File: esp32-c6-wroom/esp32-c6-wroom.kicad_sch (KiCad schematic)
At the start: 1 part, among them U1 ESP32-C6-WROOM-1-N8

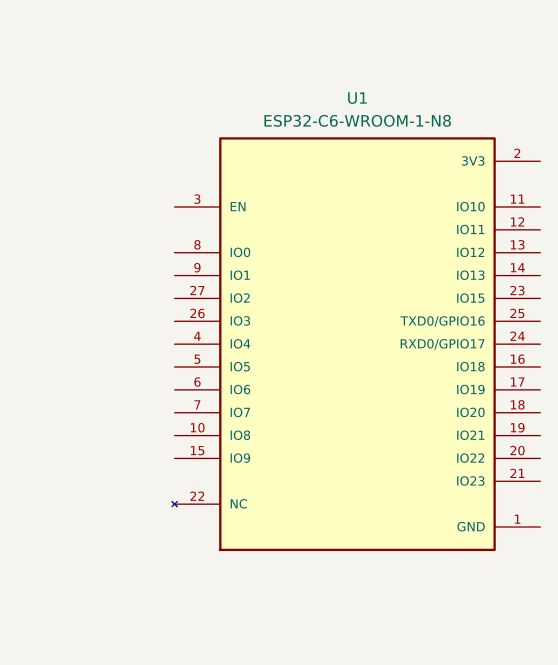
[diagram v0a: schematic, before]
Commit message: fix: use official espressif lib for esp32-c6 projects
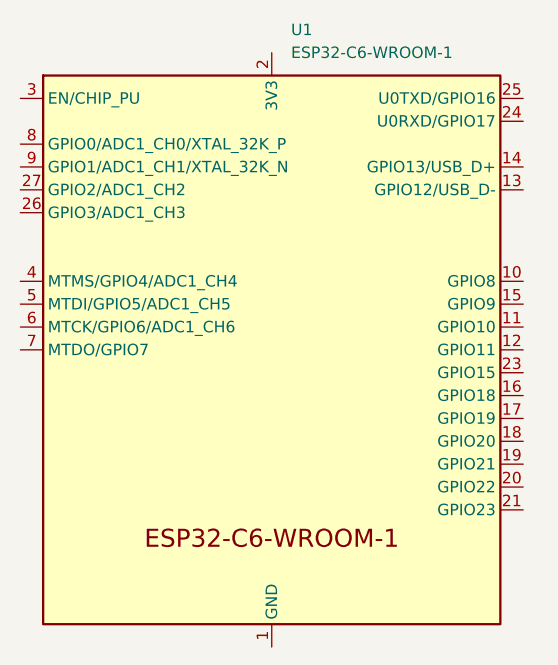
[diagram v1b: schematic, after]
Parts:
- removed U1: ESP32-C6-WROOM-1-N8, ESP32:XCVR_ESP32-C6-WROOM-1-N8, symbol ESP32:ESP32-C6-WROOM-1-N8
- added U1: ESP32-C6-WROOM-1, PCM_Espressif:ESP32-C6-WROOM-1, symbol PCM_Espressif:ESP32-C6-WROOM-1
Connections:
- new net: U1.1 (GND), U1.28 (GND), U1.29 (GND)
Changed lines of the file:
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@@
 	(paper "A4")
 	(symbol
-		(lib_id "ESP32:ESP32-C6-WROOM-1-N8")
-		(at 151.765 97.155 0)
+		(lib_id "PCM_Espressif:ESP32-C6-WROOM-1")
+		(at 142.24 97.79 0)
 		(unit 1)
 		(exclude_from_sim no)
@@
 		(fields_autoplaced yes)
 		(property "Reference" "U1"
-			(at 151.765 69.85 0)
+			(at 144.3833 62.23 0)
 			(effects
 				(font
 					(size 1.27 1.27)
 				)
+				(justify left)
 			)
 		)
-		(property "Value" "ESP32-C6-WROOM-1-N8"
-			(at 151.765 72.39 0)
+		(property "Value" "ESP32-C6-WROOM-1"
+			(at 144.3833 64.77 0)
 			(effects
 				(font
 					(size 1.27 1.27)
 				)
+				(justify left)
 			)
 		)
-		(property "Footprint" "ESP32:XCVR_ESP32-C6-WROOM-1-N8"
-			(at 151.765 97.155 0)
-			(effects
-				(font
-					(size 1.27 1.27)
-				)
-				(justify bottom)
-				(hide yes)
-			)
-		)
-		(property "Datasheet" ""
-			(at 151.765 97.155 0)
+		(property "Footprint" "PCM_Espressif:ESP32-C6-WROOM-1"
+			(at 142.24 142.875 0)
 			(effects
 				(font
@@
 			)
 		)
-		(property "Description" ""
-			(at 151.765 97.155 0)
+		(property "Datasheet" "https://www.espressif.com/sites/default/files/documentation/esp32-c6-wroom-1_wroom-1u_datasheet_en.pdf"
+			(at 142.24 146.05 0)
 			(effects
 				(font
@@
 			)
 		)
-		(property "MF" "Espressif Systems"
-			(at 151.765 97.155 0)
+		(property "Description" "ESP32-C6-WROOM-1/U is a module that supports 2.4 GHz Wi-Fi 6 (802.11 ax), Bluetooth® 5 (LE), Zigbee and Thread (802.15.4)"
+			(at 142.24 97.79 0)
 			(effects
 				(font
 					(size 1.27 1.27)
 				)
-				(justify bottom)
 				(hide yes)
 			)
 		)
-		(property "MAXIMUM_PACKAGE_HEIGHT" "3.25mm"
-			(at 151.765 97.155 0)
-			(effects
-				(font
-					(size 1.27 1.27)
-				)
-				(justify bottom)
-				(hide yes)
-			)
+		(pin "24"
 		)
-		(property "Package" "SMD-28 Espressif Systems"
-			(at 151.765 97.155 0)
-			(effects
-				(font
-					(size 1.27 1.27)
-				)
-				(justify bottom)
-				(hide yes)
-			)
+		(pin "26"
 		)
-		(property "Price" "None"
-			(at 151.765 97.155 0)
-			(effects
-				(font
-					(size 1.27 1.27)
-				)
-				(justify bottom)
-				(hide yes)
-			)
+		(pin "1"
 		)
-		(property "Check_prices" "https://www.snapeda.com/parts/ESP32-C6-WROOM-1-N8/Espressif+Systems/view-part/?ref=eda"
-			(at 151.765 97.155 0)
-			(effects
-				(font
-					(size 1.27 1.27)
-				)
-				(justify bottom)
-				(hide yes)
-			)
+		(pin "2"
 		)
-		(property "STANDARD" "Manufacturer Recommendations"
-			(at 151.765 97.155 0)
-			(effects
-				(font
-					(size 1.27 1.27)
-				)
-				(justify bottom)
-				(hide yes)
-			)
+		(pin "9"
 		)
-		(property "PARTREV" "1.0"
-			(at 151.765 97.155 0)
-			(effects
-				(font
-					(size 1.27 1.27)
-				)
-				(justify bottom)
-				(hide yes)
-			)
+		(pin "8"
 		)
-		(property "SnapEDA_Link" "https://www.snapeda.com/parts/ESP32-C6-WROOM-1-N8/Espressif+Systems/view-part/?ref=snap"
-			(at 151.765 97.155 0)
-			(effects
-				(font
-					(size 1.27 1.27)
-				)
-				(justify bottom)
-				(hide yes)
-			)
+		(pin "6"
 		)
-		(property "MP" "ESP32-C6-WROOM-1-N8"
-			(at 151.765 97.155 0)
-			(effects
-				(font
-					(size 1.27 1.27)
-				)
-				(justify bottom)
-				(hide yes)
-			)
+		(pin "22"
 		)
-		(property "Purchase-URL" "https://www.snapeda.com/api/url_track_click_mouser/?unipart_id=12616380&manufacturer=Espressif Systems&part_name=ESP32-C6-WROOM-1-N8&search_term=esp32-c6-wroom"
-			(at 151.765 97.155 0)
-			(effects
-				(font
-					(size 1.27 1.27)
-				)
-				(justify bottom)
-				(hide yes)
-			)
+		(pin "7"
 		)
-		(property "Description_1" "Multiprotocol Modules ESP32-C6 module, Wi-Fi 6 in 2.4 GHz band, Bluetooth 5, Zigbee 3.0 and Thread. ESP34-WROOM Compatible - ENGINEERING SAMPLE"
-			(at 151.765 97.155 0)
-			(effects
-				(font
-					(size 1.27 1.27)
-				)
-				(justify bottom)
-				(hide yes)
-			)
-		)
-		(property "Availability" "In Stock"
-			(at 151.765 97.155 0)
-			(effects
-				(font
-					(size 1.27 1.27)
-				)
-				(justify bottom)
-				(hide yes)
-			)
-		)
-		(property "MANUFACTURER" "Espressif Systems"
-			(at 151.765 97.155 0)
-			(effects
-				(font
-					(size 1.27 1.27)
-				)
-				(justify bottom)
-				(hide yes)
-			)
+		(pin "17"
 		)
 		(pin "13"
 		)
+		(pin "28"
+		)
 		(pin "4"
+		)
+		(pin "29"
 		)
 		(pin "27"
 		)
-		(pin "5"
+		(pin "11"
+		)
+		(pin "23"
 		)
 		(pin "3"
 		)
-		(pin "17"
+		(pin "16"
+		)
+		(pin "18"
+		)
+		(pin "25"
+		)
+		(pin "5"
+		)
+		(pin "10"
+		)
+		(pin "21"
+		)
+		(pin "12"
+		)
+		(pin "14"
+		)
+		(pin "19"
 		)
 		(pin "15"
@@
 		(pin "20"
 		)
-		(pin "1"
-		)
-		(pin "2"
-		)
-		(pin "29_3"
-		)
-		(pin "10"
-		)
-		(pin "6"
-		)
-		(pin "22"
-		)
-		(pin "11"
-		)
-		(pin "9"
-		)
-		(pin "8"
-		)
-		(pin "7"
-		)
-		(pin "26"
-		)
-		(pin "12"
-		)
-		(pin "23"
-		)
-		(pin "24"
-		)
-		(pin "25"
-		)
-		(pin "14"
-		)
-		(pin "16"
-		)
-		(pin "18"
-		)
-		(pin "19"
-		)
-		(pin "21"
-		)
-		(pin "28"
-		)
-		(pin "29_1"
-		)
-		(pin "29_2"
-		)
-		(pin "29_4"
-		)
-		(pin "29_5"
-		)
-		(pin "29_6"
-		)
-		(pin "29_7"
-		)
-		(pin "29_9"
-		)
-		(pin "29_8"
-		)
 		(instances
